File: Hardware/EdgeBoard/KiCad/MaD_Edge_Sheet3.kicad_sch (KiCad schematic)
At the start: 47 parts, among them IC14 ISO7741FDWR, IC15 ISO6721BDR, IC16 ISO6740FDWR, J20 Encoder, J21 ServoCtrl, J23 ServoSerial, Q1 MMBT3904, U24 AM26LS31CD, U25 AM26C32IDR, U27 SN74LVC1G14DBV, U28 SN74LVC1G14DBV, U29 SN74LVC1G14DBV, U30 SN74LVC1G14DBV, U31 SN74LVC1G14DBV, U32 SN74LVC1G14DBV, U33 SN74LVC1G14DBV, U34 SN74LVC1G14DBV

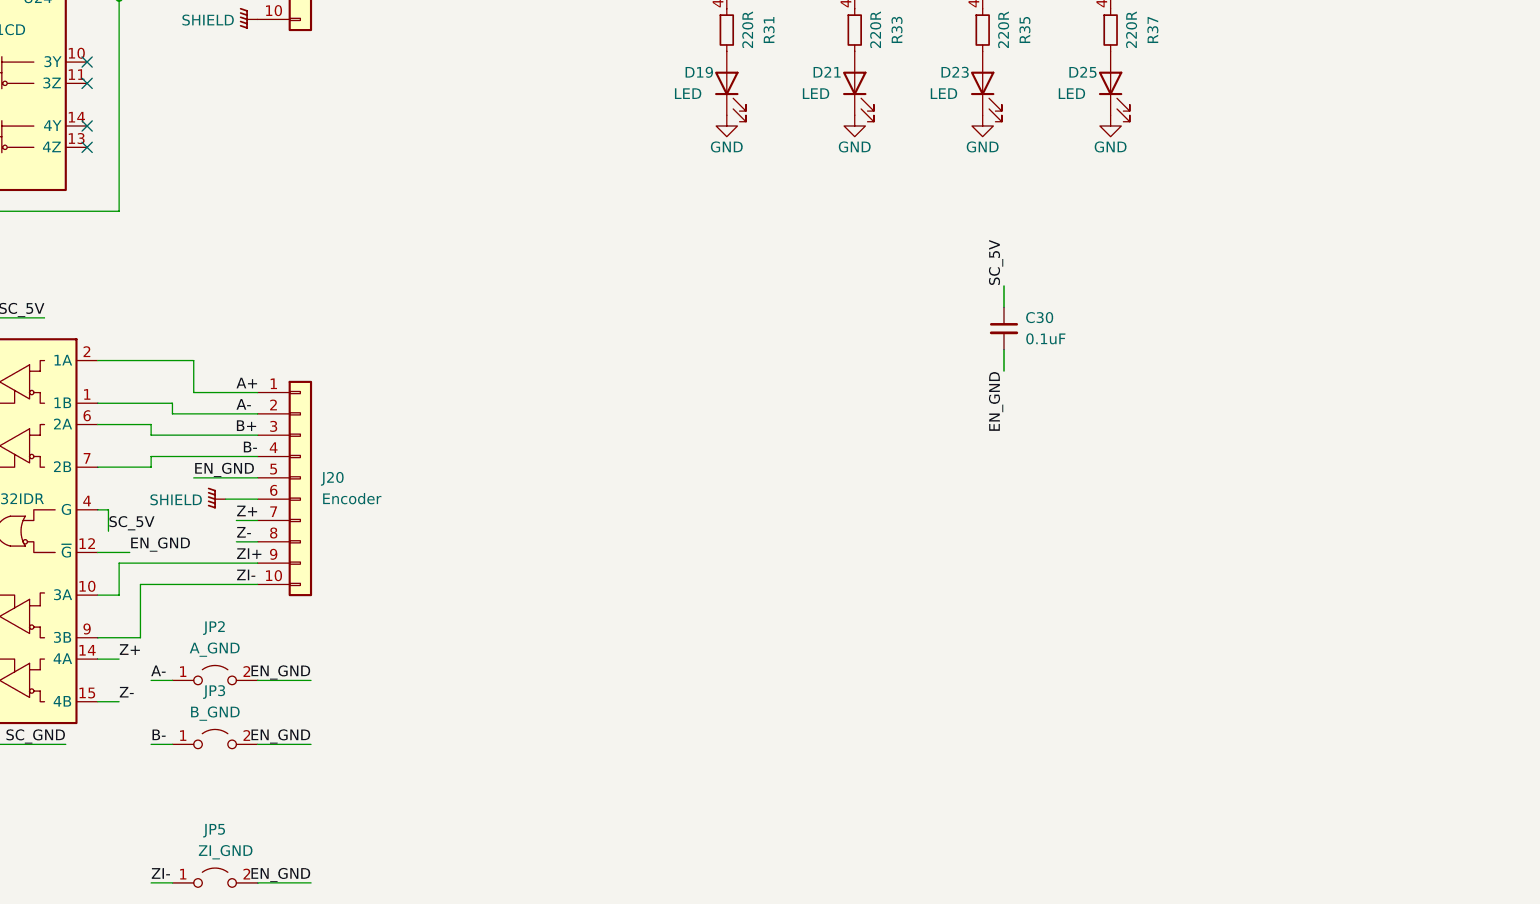
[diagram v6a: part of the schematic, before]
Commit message: feat(hardware): encoder front end for single-ended and open-collector encoders
Findings ENC-F4a and ENC-F4b. Grounding a minus input can never give the
-0.2 V differential low (SLLS104M 5.6 p.5), and the Taiss NPN
open-collector encoder had no pull-up and no supply.

- JP2/JP3/JP5 now tie A-/B-/ZI- to ENC_REF instead of EN_GND (values
  A_REF/B_REF/ZI_REF); JP6 (Z_REF) is the Z- jumper where JP4 was.
- ENC_REF = SC_5V/2: R43/R44 2.2 k, C31 0.1 uF, placed between IC14 and
  IC16; B.Cu to the four jumpers.
- R40/R41/R42 2.2 k pull-ups on A+/B+/Z+ (an A/B/Z encoder). Placed
  between J21 and J20, tapped onto the + nets with vias and B.Cu.
- J25 (1x3 header: VIN, fused +V, 0V) with F1, Littelfuse 1206L020/30NR
  (C7542932; 0.20 A hold, 30 V, 1206L datasheet p.1), as an external
  supply pass-through: J20 has no free pin and the encoder side only has
  SC_5V from the drive.
- BOM: SH1-SH4, 2.54 mm shunts (HC-JP254-1-65-CL-B-G0, C5380290) for
  JP1 (always) and JP2/JP3/JP6 (open-collector encoder only), as
  BOM-only symbols.
- Silkscreen: SERVO label moved up 2.2 mm; VIN/+V/0V at J25; SHUNT=OC
  between the jumpers.

Co-Authored-By: Claude Opus 5.5 <noreply@anthropic.com>
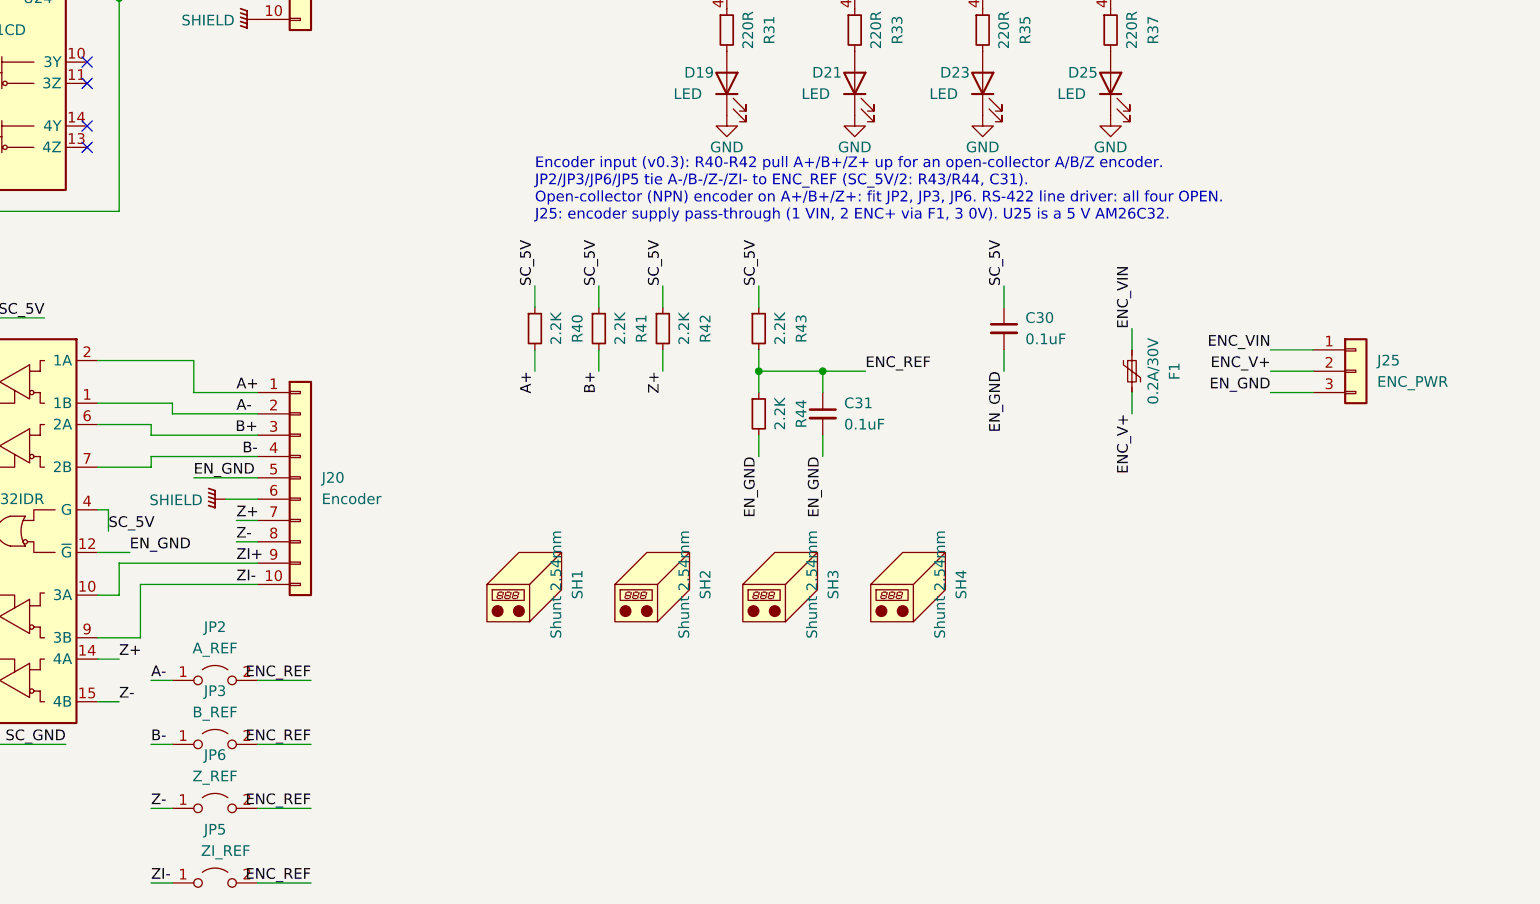
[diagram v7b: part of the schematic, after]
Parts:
- added C31: 0.1uF, Capacitor_SMD:C_0603_1608Metric, symbol Device:C_Small
- added F1: 0.2A/30V, Fuse:Fuse_1206_3216Metric, symbol Device:Polyfuse_Small
- added J25: ENC_PWR, Connector_PinHeader_2.54mm:PinHeader_1x03_P2.54mm_Vertical, symbol Connector_Generic:Conn_01x03
- added JP6: Z_REF, Connector_PinHeader_2.54mm:PinHeader_1x02_P2.54mm_Vertical, symbol Jumper:Jumper_2_Open
- added R40, R41, R42, R43, R44: 2.2K, Resistor_SMD:R_0603_1608Metric, symbol Device:R_Small
- added SH1, SH2, SH3, SH4: Shunt 2.54mm, symbol Mechanical:Housing
- JP2: value A_GND -> A_REF; NOTES (none) -> Shunt only for a single-ended open-collector encoder; OPEN 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
- JP3: value B_GND -> B_REF; NOTES (none) -> Shunt only for a single-ended open-collector encoder; OPEN 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
- JP5: value ZI_GND -> ZI_REF; NOTES (none) -> Shunt only for a single-ended push-pull (TTL) ZI signal; OP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
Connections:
- net A+: now also R40.2
- net B+: now also R41.2
- net EN_GND: now also C31.2, J25.3 (Pin_3), R44.2; no longer JP2.2 (B), JP3.2 (B), JP5.2 (B)
- net SC_5V: now also R40.1, R41.1, R42.1, R43.1
- net Z+: now also R42.2
- net Z-: now also JP6.1 (A)
- new net ENC_REF: C31.1, JP2.2 (B), JP3.2 (B), JP5.2 (B), JP6.2 (B), R43.2, R44.1
- new net ENC_V+: F1.2, J25.2 (Pin_2)
- new net ENC_VIN: F1.1, J25.1 (Pin_1)
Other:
- note added: "Encoder input (v0.3): R40-R42 pull A+/B+/Z+ up for an open-collector A/B/Z encoder. JP2/JP3/JP6/JP5 tie A-/B-/Z-/ZI- to ENC_REF (SC_5V/2: R43/R44, C31). Open-collector (NPN) encoder on A+/B+/Z+: fit JP2, JP3, JP6. RS-422 line driver: all four OPEN. J25: encoder supply pass-through (1 VIN, 2 ENC+ via F1, 3 0V). U25 is a 5 V AM26C32."
